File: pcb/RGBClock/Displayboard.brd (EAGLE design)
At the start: 100 x 80 mm, 60 parts, among them IC1 MCP23017SO, U1 LP3878MR-ADJ, U2 P82B96DR, U3 P82B96DR, U4 PCA9685PW, U5 TPS71533DCKR, U6 ZXLD1362ET5TA, X1 5566-4, X4 1503_09

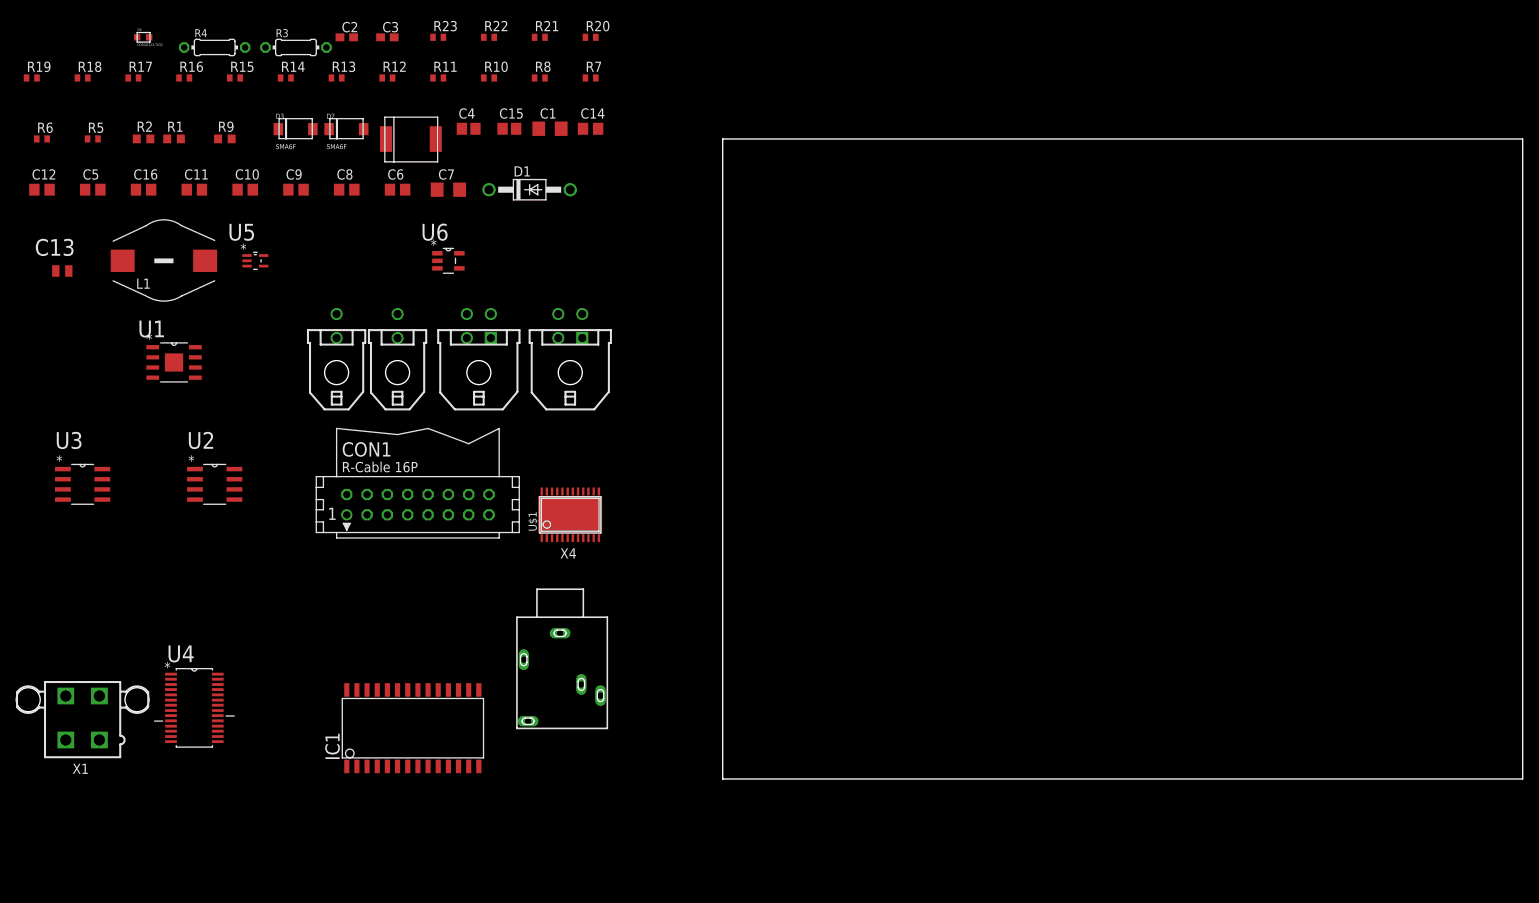
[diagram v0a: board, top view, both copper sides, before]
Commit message: 
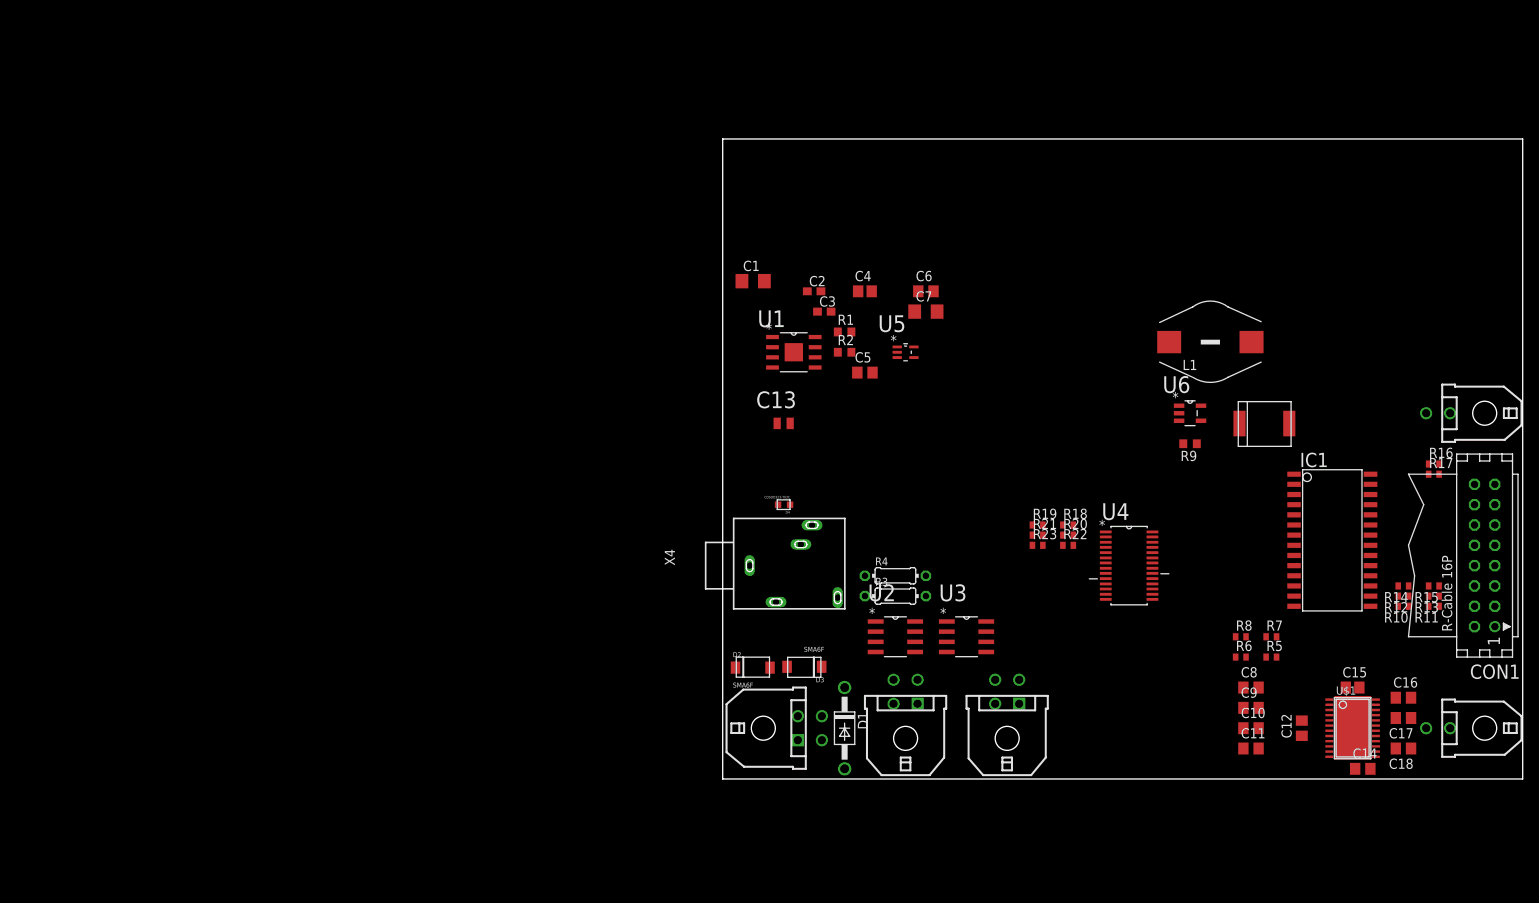
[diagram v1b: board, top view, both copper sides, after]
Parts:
- removed X1: 5566-4, con-molex:5566-4
- added C17, C18: 0.47u, rcl:C0805
- added X7: (no value), con-molex-micro-fit-3_0:43045-0400
- R10: value A1-1 -> A0-1
- R11: value A1-0 -> A0-0
- R12: value A0-1 -> A1-1
- R13: value A0-0 -> A1-0
- R14: value A0-1 -> A2-1
- R15: value A0-0 -> A2-0
- moved C12 171.3 mm to (72.4, 6.35), turned to 90 degrees
- moved R17 169.9 mm to (88.9, 38.1)
- moved C16 169.8 mm to (85.1, 10.2)
- moved R16 163.5 mm to (88.9, 39.4)
- moved R6 163.3 mm to (64.8, 15.2)
- moved R15 162.8 mm to (88.9, 24.1), turned to 180 degrees
- moved R5 160.9 mm to (68.6, 15.2)
- moved R14 153.5 mm to (85.1, 24.1), turned to 180 degrees
- moved R13 151.7 mm to (88.9, 22.9), turned to 180 degrees
- moved C11 149.4 mm to (66.0, 3.81)
- moved X6 143.6 mm to (95.2, 45.7), turned to 90 degrees
- moved X5 143.0 mm to (95.2, 6.35), turned to 90 degrees
- moved C10 142.6 mm to (66.0, 6.35)
- moved R12 142.6 mm to (85.1, 22.9), turned to 180 degrees
- moved R11 140.9 mm to (88.9, 21.6), turned to 180 degrees
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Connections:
- net N$4 renamed RW
- net N$5 renamed RS
- net N$7 renamed E
- removed net D8: CON1.14, IC1.28
- new net D0: CON1.7, IC1.21
- new net N$4: C18.1, U$1.17
- new net N$5: C17.1, U$1.18
- net D1: now also CON1.8, IC1.22; no longer CON1.7, IC1.21
- net D2: now also CON1.9, IC1.23; no longer CON1.8, IC1.22
- net D3: now also CON1.10, IC1.24; no longer CON1.9, IC1.23
- net D4: now also CON1.11, IC1.25; no longer CON1.10, IC1.24
- net D5: now also CON1.12, IC1.26; no longer CON1.11, IC1.25
- net D6: now also CON1.13, IC1.27; no longer CON1.12, IC1.26
- net D7: now also CON1.14, IC1.28; no longer CON1.13, IC1.27
- net GND: now also C17.2, C18.2, X7.P$1; no longer U$1.17, U$1.18, X1.3
- net N$2: now also X7.P$3; no longer X1.2
- net N$22: now also X7.P$2; no longer X1.1
- net N$25: now also X7.P$4; no longer X1.4

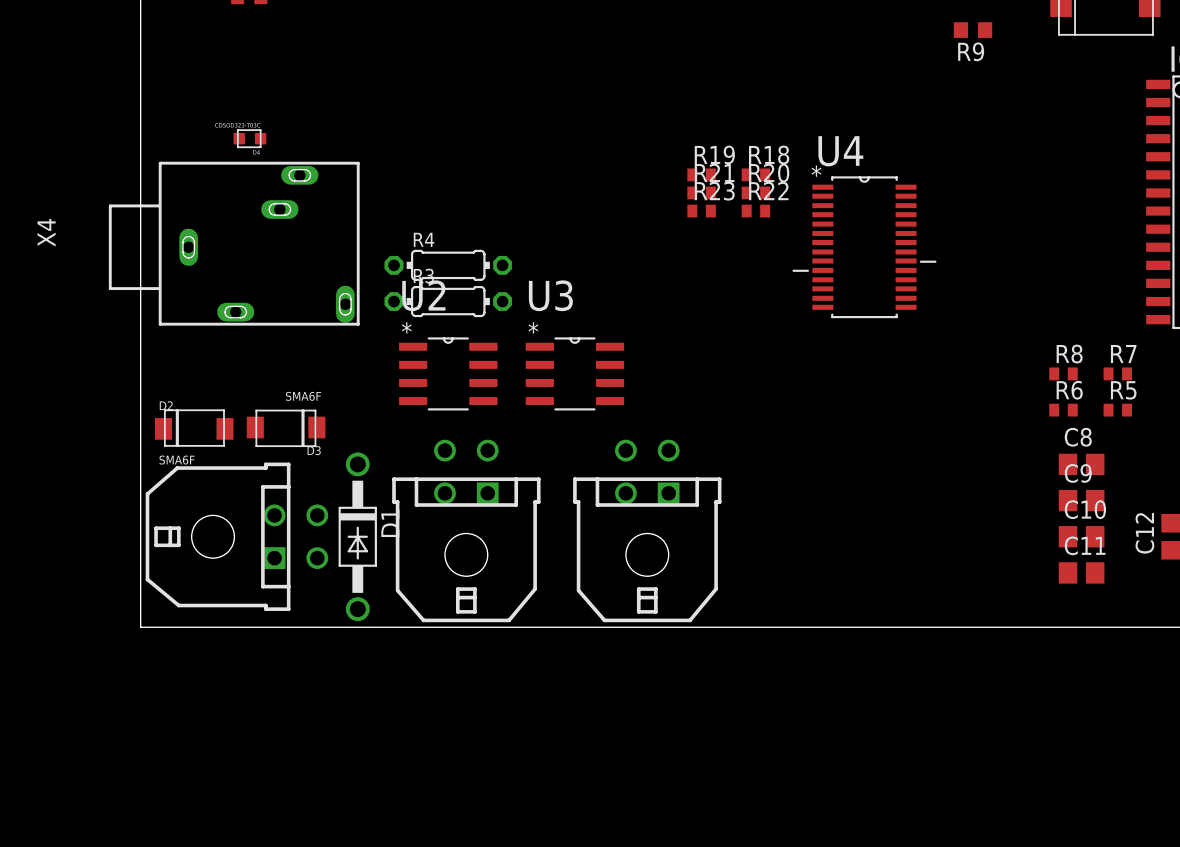
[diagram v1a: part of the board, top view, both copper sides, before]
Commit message: 
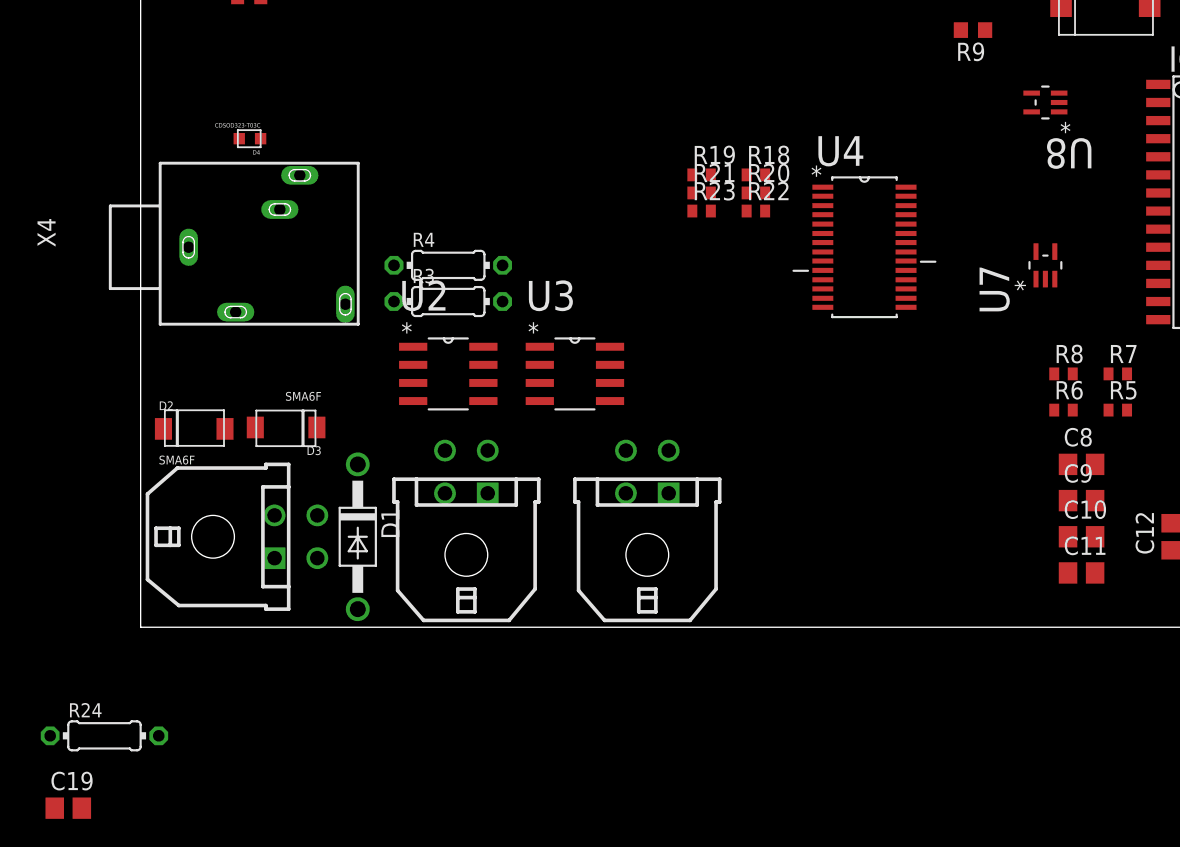
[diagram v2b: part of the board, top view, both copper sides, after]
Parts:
- added C19: 22n, rcl:C0805
- added R24: 3300, rcl:0204/7
- added U7: 74HCT1G14GW, NXP_By_element14_Batch_1:SOT65P210X110-5N
- added U8: 74HCT1G86GW, NXP_By_element14_Batch_1:SOT65P210X110-5N
- X2, X3, X7: value (none) -> 43045-0400
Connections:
- removed net E: CON1.6, IC1.3
- new net N$3: IC1.3, R24.2, U8.2
- new net N$30: C19.2, R24.1, U7.2
- new net N$31: U7.4, U8.1
- new net N$32: CON1.6, U8.4
- net +5V: now also IC1.18, U7.5, U8.5
- net GND: now also C19.1, U7.3, U8.3
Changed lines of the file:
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@@
 </element>
 <element name="D4" library="MyComponents" package="SOD323" value="CDSOD323-T03C" x="7.62" y="34.29" rot="R180"/>
-<element name="X2" library="con-molex-micro-fit-3_0" package="43045-0400" value="" x="35.56" y="5.08">
+<element name="X2" library="con-molex-micro-fit-3_0" package="43045-0400" value="43045-0400" x="35.56" y="5.08">
 <attribute name="MATERIAL" value="" x="54.61" y="-45.72" size="1.778" layer="27" display="off"/>
 </element>
-<element name="X3" library="con-molex-micro-fit-3_0" package="43045-0400" value="" x="22.86" y="5.08">
+<element name="X3" library="con-molex-micro-fit-3_0" package="43045-0400" value="43045-0400" x="22.86" y="5.08">
 <attribute name="MATERIAL" value="" x="53.34" y="-45.72" size="1.778" layer="27" display="off"/>
 </element>
@@
 <element name="C17" library="rcl" package="C0805" value="0.47u" x="85.09" y="7.62" rot="R180"/>
 <element name="C18" library="rcl" package="C0805" value="0.47u" x="85.09" y="3.81" rot="R180"/>
-<element name="X7" library="con-molex-micro-fit-3_0" package="43045-0400" value="" x="5.08" y="6.35" rot="R270">
+<element name="X7" library="con-molex-micro-fit-3_0" package="43045-0400" value="43045-0400" x="5.08" y="6.35" rot="R270">
 <attribute name="MATERIAL" value="" x="5.08" y="6.35" size="1.778" layer="27" rot="R270" display="off"/>
 </element>
+<element name="U7" library="NXP_By_element14_Batch_1" package="SOT65P210X110-5N" value="74HCT1G14GW" x="63.5" y="25.4" rot="R90">
+<attribute name="PACKAGE" value="SOT-5" x="63.5" y="25.4" size="1.778" layer="27" rot="R90" display="off"/>
+<attribute name="OC_NEWARK" value="99K0543" x="63.5" y="25.4" size="1.778" layer="27" rot="R90" display="off"/>
+<attribute name="MPN" value="74HCT1G14GW" x="63.5" y="25.4" size="1.778" layer="27" rot="R90" display="off"/>
+<attribute name="SUPPLIER" value="NXP" x="63.5" y="25.4" size="1.778" layer="27" rot="R90" display="off"/>
+<attribute name="OC_FARNELL" value="1085264" x="63.5" y="25.4" size="1.778" layer="27" rot="R90" display="off"/>
+</element>
+<element name="U8" library="NXP_By_element14_Batch_1" package="SOT65P210X110-5N" value="74HCT1G86GW" x="63.5" y="36.83" rot="R180">
+<attribute name="PACKAGE" value="SOT-5" x="63.5" y="36.83" size="1.778" layer="27" rot="R180" display="off"/>
+<attribute name="OC_NEWARK" value="99K0545" x="63.5" y="36.83" size="1.778" layer="27" rot="R180" display="off"/>
+<attribute name="MPN" value="74HCT1G86GW" x="63.5" y="36.83" size="1.778" layer="27" rot="R180" display="off"/>
+<attribute name="SUPPLIER" value="NXP" x="63.5" y="36.83" size="1.778" layer="27" rot="R180" display="off"/>
+<attribute name="OC_FARNELL" value="1085266" x="63.5" y="36.83" size="1.778" layer="27" rot="R180" display="off"/>
+</element>
+<element name="R24" library="rcl" package="0204/7" value="3300" x="-2.54" y="-7.62"/>
+<element name="C19" library="rcl" package="C0805" value="22n" x="-5.08" y="-12.7"/>
 </elements>
 <signals>
@@
 <contactref element="C17" pad="2"/>
 <contactref element="X7" pad="P$1"/>
+<contactref element="U7" pad="3"/>
+<contactref element="U8" pad="3"/>
+<contactref element="C19" pad="1"/>
 <wire x1="89.55" y1="21.59" x2="96.52" y2="19.05" width="0" layer="19" extent="1-1"/>
 <wire x1="89.55" y1="22.86" x2="89.55" y2="21.59" width="0" layer="19" extent="1-1"/>
@@
 <wire x1="64.12" y1="15.24" x2="65.09" y2="11.43" width="0" layer="19" extent="1-1"/>
 <wire x1="64.12" y1="17.78" x2="64.12" y2="15.24" width="0" layer="19" extent="1-1"/>
-<wire x1="71.42" y1="26.67" x2="64.12" y2="17.78" width="0" layer="19" extent="1-1"/>
-<wire x1="53.721" y1="27.6352" x2="64.12" y2="17.78" width="0" layer="19" extent="1-1"/>
+<wire x1="64.1604" y1="24.4348" x2="64.12" y2="17.78" width="0" layer="19" extent="1-1"/>
+<wire x1="71.42" y1="26.67" x2="64.1604" y2="24.4348" width="0" layer="19" extent="1-1"/>
+<wire x1="53.721" y1="27.6352" x2="64.1604" y2="24.4348" width="0" layer="19" extent="1-1"/>
 <wire x1="53.721" y1="28.2956" x2="53.721" y2="27.6352" width="0" layer="19" extent="1-1"/>
 <wire x1="53.721" y1="28.956" x2="53.721" y2="28.2956" width="0" layer="19" extent="1-1"/>
@@
 <wire x1="38.72" y1="31.75" x2="38.72" y2="29.21" width="0" layer="19" extent="1-1"/>
 <wire x1="47.879" y1="22.4536" x2="47.879" y2="28.2956" width="0" layer="19" extent="1-1"/>
-<wire x1="57.0484" y1="45.72" x2="53.721" y2="28.956" width="0" layer="19" extent="1-1"/>
+<wire x1="64.4652" y1="37.4904" x2="71.42" y2="26.67" width="0" layer="19" extent="1-1"/>
+<wire x1="57.0484" y1="45.72" x2="64.4652" y2="37.4904" width="0" layer="19" extent="1-1"/>
 <wire x1="28.0162" y1="15.875" x2="38.72" y2="29.21" width="0" layer="19" extent="1-1"/>
 <wire x1="34.06" y1="12.4" x2="28.0162" y2="15.875" width="0" layer="19" extent="1-1"/>
@@
 <wire x1="12.28" y1="60.96" x2="18.63" y2="60.96" width="0" layer="19" extent="1-1"/>
 <wire x1="5.21" y1="62.23" x2="12.28" y2="60.96" width="0" layer="19" extent="1-1"/>
+<wire x1="-6.03" y1="-12.7" x2="9.4" y2="4.85" width="0" layer="19" extent="1-1"/>
 </signal>
 <signal name="VCC" class="2">
@@
 <contactref element="U$1" pad="19"/>
 <contactref element="U$1" pad="16"/>
+<contactref element="U8" pad="5"/>
+<contactref element="U7" pad="5"/>
+<contactref element="IC1" pad="18"/>
 <wire x1="84.44" y1="21.59" x2="93.98" y2="19.05" width="0" layer="19" extent="1-1"/>
 <wire x1="84.44" y1="22.86" x2="84.44" y2="21.59" width="0" layer="19" extent="1-1"/>
 <wire x1="84.44" y1="24.13" x2="84.44" y2="22.86" width="0" layer="19" extent="1-1"/>
-<wire x1="77.89" y1="11.43" x2="84.44" y2="21.59" width="0" layer="19" extent="1-1"/>
+<wire x1="80.98" y1="25.4" x2="84.44" y2="24.13" width="0" layer="19" extent="1-1"/>
+<wire x1="71.42" y1="27.94" x2="80.98" y2="25.4" width="0" layer="19" extent="1-1"/>
+<wire x1="62.8396" y1="26.3652" x2="71.42" y2="27.94" width="0" layer="19" extent="1-1"/>
+<wire x1="62.5348" y1="36.1696" x2="62.8396" y2="26.3652" width="0" layer="19" extent="1-1"/>
+<wire x1="53.721" y1="30.8864" x2="62.8396" y2="26.3652" width="0" layer="19" extent="1-1"/>
+<wire x1="43.83" y1="30.48" x2="53.721" y2="30.8864" width="0" layer="19" extent="1-1"/>
+<wire x1="43.83" y1="31.75" x2="43.83" y2="30.48" width="0" layer="19" extent="1-1"/>
+<wire x1="40.02" y1="30.48" x2="43.83" y2="30.48" width="0" layer="19" extent="1-1"/>
+<wire x1="69.23" y1="17.78" x2="71.42" y2="27.94" width="0" layer="19" extent="1-1"/>
+<wire x1="69.23" y1="15.24" x2="69.23" y2="17.78" width="0" layer="19" extent="1-1"/>
+<wire x1="77.89" y1="11.43" x2="69.23" y2="15.24" width="0" layer="19" extent="1-1"/>
 <wire x1="81.6578" y1="8.625" x2="77.89" y2="11.43" width="0" layer="19" extent="1-1"/>
 <wire x1="81.6578" y1="7.325" x2="81.6578" y2="8.625" width="0" layer="19" extent="1-1"/>
@@
 <wire x1="75.8222" y1="5.375" x2="79.06" y2="1.27" width="0" layer="19" extent="1-1"/>
 <wire x1="72.39" y1="5.4" x2="75.8222" y2="5.375" width="0" layer="19" extent="1-1"/>
-<wire x1="69.23" y1="15.24" x2="77.89" y2="11.43" width="0" layer="19" extent="1-1"/>
-<wire x1="69.23" y1="17.78" x2="69.23" y2="15.24" width="0" layer="19" extent="1-1"/>
-<wire x1="71.42" y1="27.94" x2="69.23" y2="17.78" width="0" layer="19" extent="1-1"/>
-<wire x1="53.721" y1="30.8864" x2="71.42" y2="27.94" width="0" layer="19" extent="1-1"/>
-<wire x1="43.83" y1="30.48" x2="53.721" y2="30.8864" width="0" layer="19" extent="1-1"/>
-<wire x1="43.83" y1="31.75" x2="43.83" y2="30.48" width="0" layer="19" extent="1-1"/>
-<wire x1="40.02" y1="30.48" x2="43.83" y2="30.48" width="0" layer="19" extent="1-1"/>
 <wire x1="25.4" y1="25.4" x2="40.02" y2="30.48" width="0" layer="19" extent="1-1"/>
 <wire x1="25.4" y1="22.86" x2="25.4" y2="25.4" width="0" layer="19" extent="1-1"/>
@@
 <wire x1="71.42" y1="36.83" x2="96.52" y2="24.13" width="0" layer="19" extent="1-1"/>
 </signal>
-<signal name="E">
-<contactref element="IC1" pad="3"/>
-<contactref element="CON1" pad="6"/>
-<wire x1="71.42" y1="35.56" x2="93.98" y2="24.13" width="0" layer="19" extent="1-1"/>
-</signal>
 <signal name="N$4">
 <contactref element="U$1" pad="17"/>
@@
 </signal>
 <signal name="N$7">
-<contactref element="X3" pad="P$2"/>
 <contactref element="U3" pad="1"/>
 <contactref element="X2" pad="P$2"/>
+<contactref element="X3" pad="P$2"/>
 <wire x1="34.06" y1="9.4" x2="28.0162" y2="19.685" width="0" layer="19" extent="1-1"/>
 <wire x1="21.36" y1="9.4" x2="28.0162" y2="19.685" width="0" layer="19" extent="1-1"/>
 </signal>
+<signal name="N$3">
+<contactref element="IC1" pad="3"/>
+<contactref element="U8" pad="2"/>
+<contactref element="R24" pad="2"/>
+<wire x1="64.4652" y1="36.83" x2="71.42" y2="35.56" width="0" layer="19" extent="1-1"/>
+<wire x1="1.27" y1="-7.62" x2="64.4652" y2="36.83" width="0" layer="19" extent="1-1"/>
+</signal>
+<signal name="N$30">
+<contactref element="U7" pad="2"/>
+<contactref element="R24" pad="1"/>
+<contactref element="C19" pad="2"/>
+<wire x1="-6.35" y1="-7.62" x2="63.5" y2="24.4348" width="0" layer="19" extent="1-1"/>
+<wire x1="-4.13" y1="-12.7" x2="-6.35" y2="-7.62" width="0" layer="19" extent="1-1"/>
+</signal>
+<signal name="N$31">
+<contactref element="U7" pad="4"/>
+<contactref element="U8" pad="1"/>
+<wire x1="64.1604" y1="26.3652" x2="64.4652" y2="36.1696" width="0" layer="19" extent="1-1"/>
+</signal>
+<signal name="N$32">
+<contactref element="U8" pad="4"/>
+<contactref element="CON1" pad="6"/>
+<wire x1="62.5348" y1="37.4904" x2="93.98" y2="24.13" width="0" layer="19" extent="1-1"/>
+</signal>
 </signals>
